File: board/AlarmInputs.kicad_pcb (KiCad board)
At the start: 2 copper layers, 71.1 x 81.3 mm, 14 parts, among them J1 External Devices, J2 Inputs, J3 Inputs, J4 Inputs, J5 Inputs, J6 4-Wire Connections, J7 Barrel_Jack_Switch, K1 G5Q-1A, K2 G5Q-1A, U1 Pico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

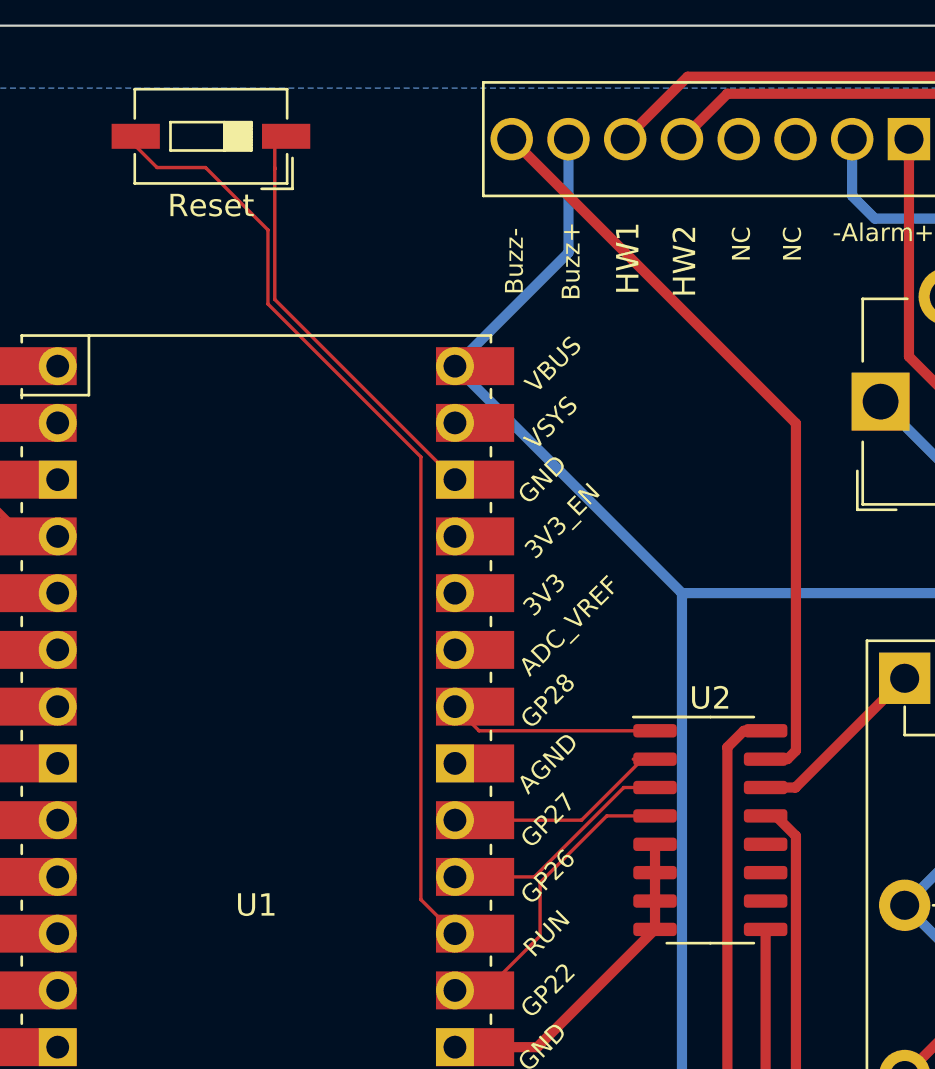
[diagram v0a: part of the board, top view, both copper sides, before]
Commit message: direct buzzer connection as darlington pair slews out the square wave too much
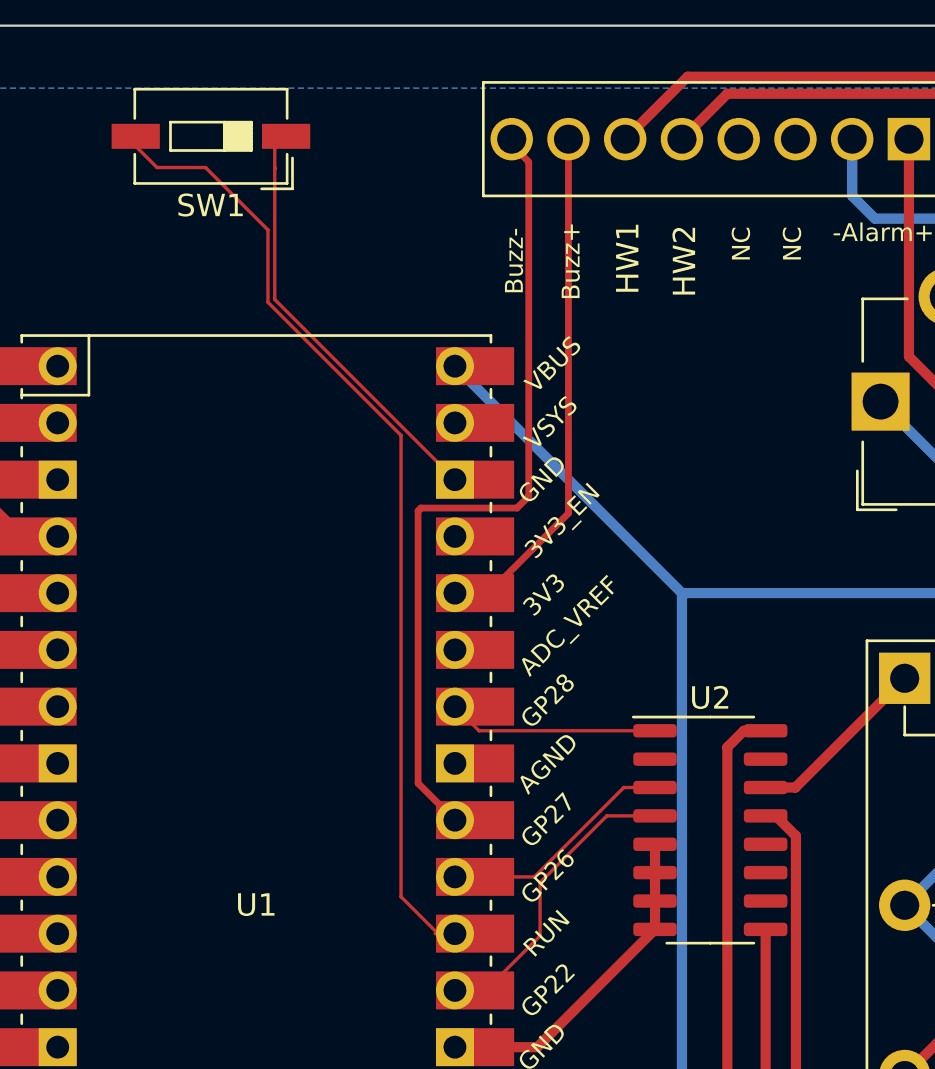
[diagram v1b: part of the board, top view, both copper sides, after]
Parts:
- renumbered Reset to SW1
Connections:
- J1 pad 7: 5V -> 3.3V
- U1 pad 32: Net-(U1-Pad32) -> BUZZERGND
- U1 pad 36: Net-(U1-Pad36) -> 3.3V
- U2 pad 15: BUZZERGND -> (no net)
- U2 pad 2: Net-(U1-Pad32) -> (no net)
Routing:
- net 3.3V: track 0.00 -> 23.3 mm
- net 5V: track 162.3 -> 150.0 mm
- net Net-(U1-Pad32): track 11.1 -> 0.00 mm
- net BUZZERGND: track 34.2 -> 35.8 mm
- net RST: track 42.9 -> 44.2 mm
